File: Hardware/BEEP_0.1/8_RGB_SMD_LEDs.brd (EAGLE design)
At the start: 84.7 x 35.6 mm, 37 parts

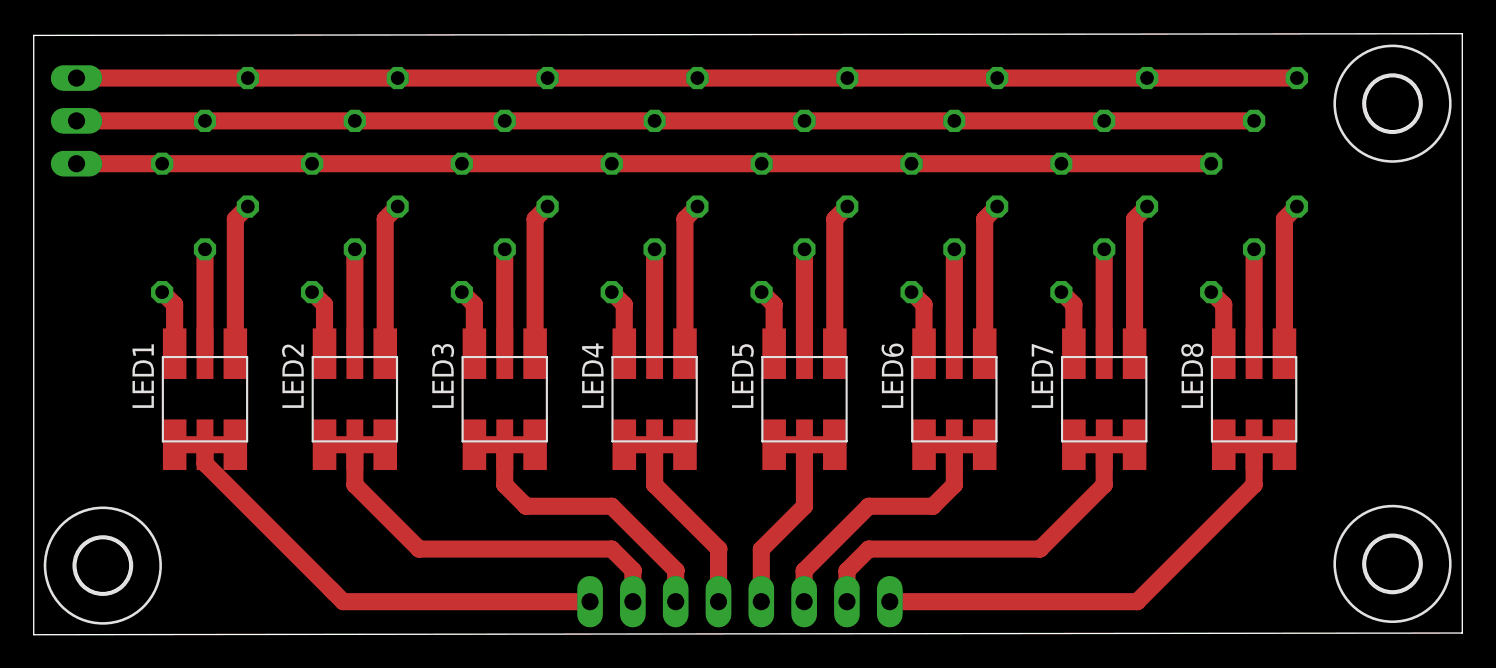
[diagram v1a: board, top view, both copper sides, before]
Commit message: Add branding ;) enhance PCBs finish Easy RGB Board add Texas Instruments libray from Element 14 add dxf import ulp for eagle add Script for easy eagle export to pdf for etching minor cleanup
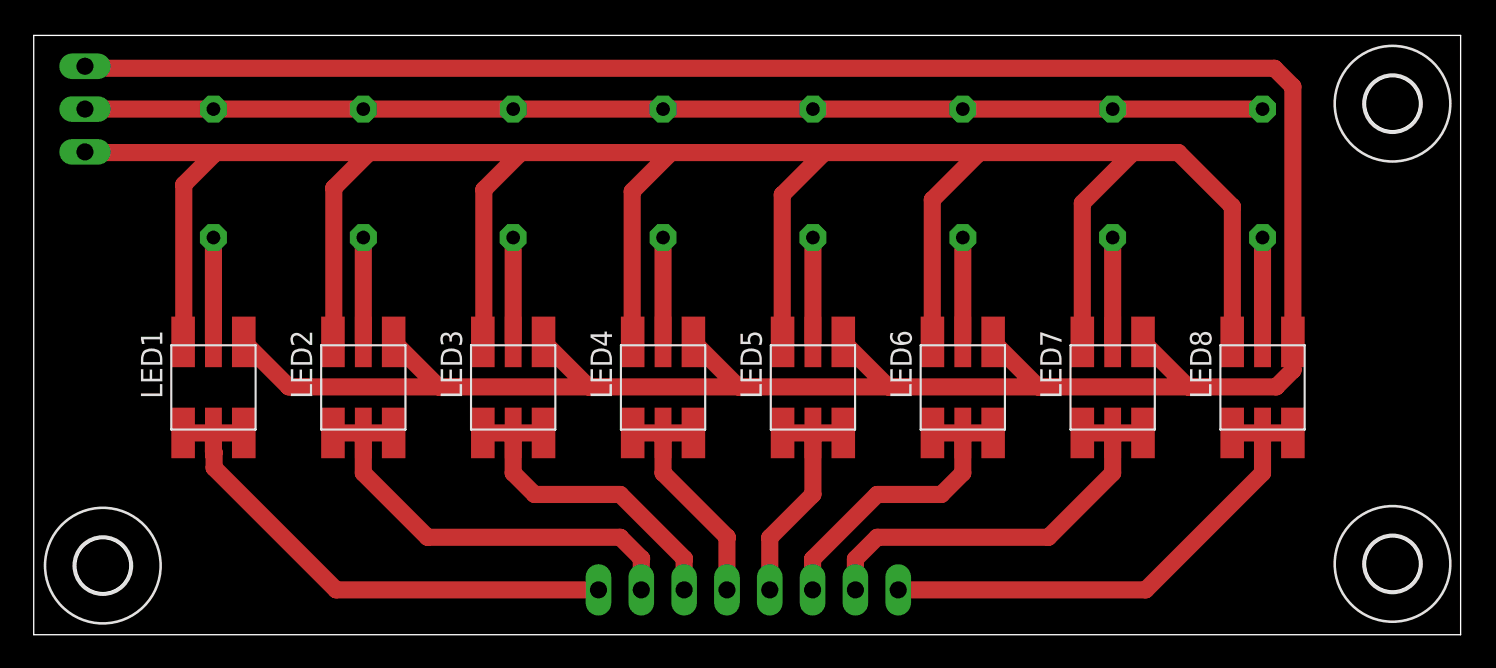
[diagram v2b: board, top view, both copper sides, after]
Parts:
- removed R1, R10, R11, R12, R13, R14, R15, R16, R17, R18, R19, R2, R20, R21, R22, R23, R24, R3, R4, R5, R6, R7, R8, R9: (no value), rcl:0207/7
- added J1, J2, J3, J4, J5, J6, J7, J8: J7MM, jumper:07
- added U$5: LOGO-COPPER7, Branding:COPPER7
- moved JP1 0.86 mm to (42.4, 2.66)
- moved LED1 0.86 mm to (10.7, 14.7)
- moved LED2 0.86 mm to (19.6, 14.7)
- moved LED3 0.86 mm to (28.4, 14.7)
- moved LED4 0.86 mm to (37.3, 14.7)
- moved LED5 0.86 mm to (46.2, 14.7)
- moved LED6 0.86 mm to (55.1, 14.7)
- moved LED7 0.86 mm to (64.0, 14.7)
- moved LED8 0.86 mm to (72.9, 14.7)
- moved RGB 0.86 mm to (3.04, 31.2)
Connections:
- removed net N$1: R1.2, R10.2, R13.2, R16.2, R19.2, R22.2, R4.2, R7.2, RGB.3
- removed net N$11: LED2.R1, R4.1
- removed net N$13: LED2.B1, R6.1
- removed net N$18: LED3.R1, R7.1
- removed net N$20: LED3.B1, R9.1
- removed net N$21: LED4.R1, R10.1
- removed net N$23: LED4.B1, R12.1
- removed net N$24: LED5.R1, R13.1
- removed net N$26: LED5.B1, R15.1
- removed net N$27: LED6.R1, R16.1
- removed net N$29: LED6.B1, R18.1
- removed net N$3: R12.2, R15.2, R18.2, R21.2, R24.2, R3.2, R6.2, R9.2, RGB.1
- removed net N$30: LED7.R1, R19.1
- removed net N$32: LED7.B1, R21.1
- removed net N$4: LED1.R1, R1.1
- removed net N$6: LED1.B1, R3.1
- net N$12: now also J2.1; no longer R5.1
- net N$19: now also J3.1; no longer R8.1
- net N$2: now also J1.2, J2.2, J3.2, J4.2, J5.2, J6.2, J7.2, J8.2; no longer R11.2, R14.2, R17.2, R2.2, R20.2, R23.2, R5.2, R8.2
- net N$22: now also J4.1; no longer R11.1
- net N$25: now also J5.1; no longer R14.1
- net N$28: now also J6.1; no longer R17.1
- net N$31: now also J7.1; no longer R20.1
- net N$33: now also LED1.R1, LED2.R1, LED3.R1, LED4.R1, LED5.R1, LED6.R1, LED7.R1, RGB.3; no longer R22.1
- net N$34: now also J8.1; no longer R23.1
- net N$35: now also LED1.B1, LED2.B1, LED3.B1, LED4.B1, LED5.B1, LED6.B1, LED7.B1, RGB.1; no longer R24.1
- net N$5: now also J1.1; no longer R2.1
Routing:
- net N$33: track 9.04 -> 175.4 mm
- net N$35: track 3.96 -> 163.1 mm
- net N$1: track 72.4 -> 0.00 mm
- net N$3: track 67.3 -> 0.00 mm
- net N$30: track 9.04 -> 0.00 mm
- net N$27: track 9.04 -> 0.00 mm
- net N$18: track 9.04 -> 0.00 mm
- net N$4: track 9.04 -> 0.00 mm
- net N$11: track 9.04 -> 0.00 mm
- net N$24: track 9.04 -> 0.00 mm
- net N$21: track 9.04 -> 0.00 mm
- net N$32: track 3.96 -> 0.00 mm
- net N$29: track 3.96 -> 0.00 mm
- net N$26: track 3.96 -> 0.00 mm
- net N$23: track 3.96 -> 0.00 mm
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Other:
- board size 84.7 x 35.6 mm -> 84.6 x 35.5 mm
- board text added: "RGB SMD 0.1.1"
